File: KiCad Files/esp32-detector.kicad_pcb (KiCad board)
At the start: 4 copper layers, 89 parts, among them IC1 MC34119, J1 Coils Connector, J2 INTERFACE, U1 4066, U2 MCP602, U3 MCP602, U4 MCP602, U5 ESP32-WROOM-32, U6 LD1117S50TR, U7 LD1117S33TR

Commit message: Upload Schematic and PCB files
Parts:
- moved U6 45.5 mm to (74.2, 61.3)
- moved R30 36.7 mm to (107.1, 48.5), turned to 0 degrees
- moved H3 35.4 mm to (124.0, 70.0)
- moved R6 35.0 mm to (110.0, 28.6), turned to 180 degrees
- moved C2 34.2 mm to (115.0, 30.0)
- moved H2 34.1 mm to (124.0, 27.0)
- moved R29 32.5 mm to (107.1, 51.6)
- moved R7 32.4 mm to (115.0, 36.0), turned to 90 degrees
- moved C13 25.2 mm to (116.3, 40.6)
- moved C40 24.0 mm to (103.8, 41.0), turned to 0 degrees
- moved C39 23.9 mm to (103.8, 44.7), turned to 180 degrees
- moved C28 23.9 mm to (112.4, 45.2), turned to -90 degrees
- moved J2 23.4 mm to (103.9, 63.8)
- moved U7 22.7 mm to (114.0, 58.7)
- moved C38 21.9 mm to (119.6, 54.9)
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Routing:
- net /IO27: track 4.15 -> 60.6 mm, vias 0 -> 2
- net /EN: track 0.00 -> 51.9 mm, vias 0 -> 1
- net /TX_PIN: track 0.00 -> 49.8 mm, vias 0 -> 2
- net GND: track 65.4 -> 89.9 mm, vias 32 -> 39
- net /SENSOR_VN: track 0.00 -> 24.2 mm, vias 0 -> 1
- net Net-(C8-Pad1): track 0.00 -> 21.5 mm, vias 0 -> 1
- net Net-(C39-Pad1): track 0.00 -> 19.8 mm
- net RX_R: track 12.2 -> 28.6 mm, vias 0 -> 1
- net Net-(C2-Pad1): track 0.00 -> 16.2 mm, vias 0 -> 1
- net Vref: track 0.00 -> 15.3 mm, vias 0 -> 1
- net /IO0: track 4.96 -> 19.2 mm
- net /+3V3: track 18.4 -> 4.24 mm, vias 0 -> 1
- net Net-(C2-Pad2): track 0.00 -> 13.7 mm
- net /TXD: track 0.00 -> 11.6 mm
- net +5V: track 19.0 -> 8.47 mm, vias 4 -> 2
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- added copper zone on B.Cu, net +12V
- added copper zone on B.Cu, net +5V
- added copper zone on B.Cu, net /+3V3
- added copper zone on In1.Cu, net GND
- removed copper zone on In1.Cu, net +5V

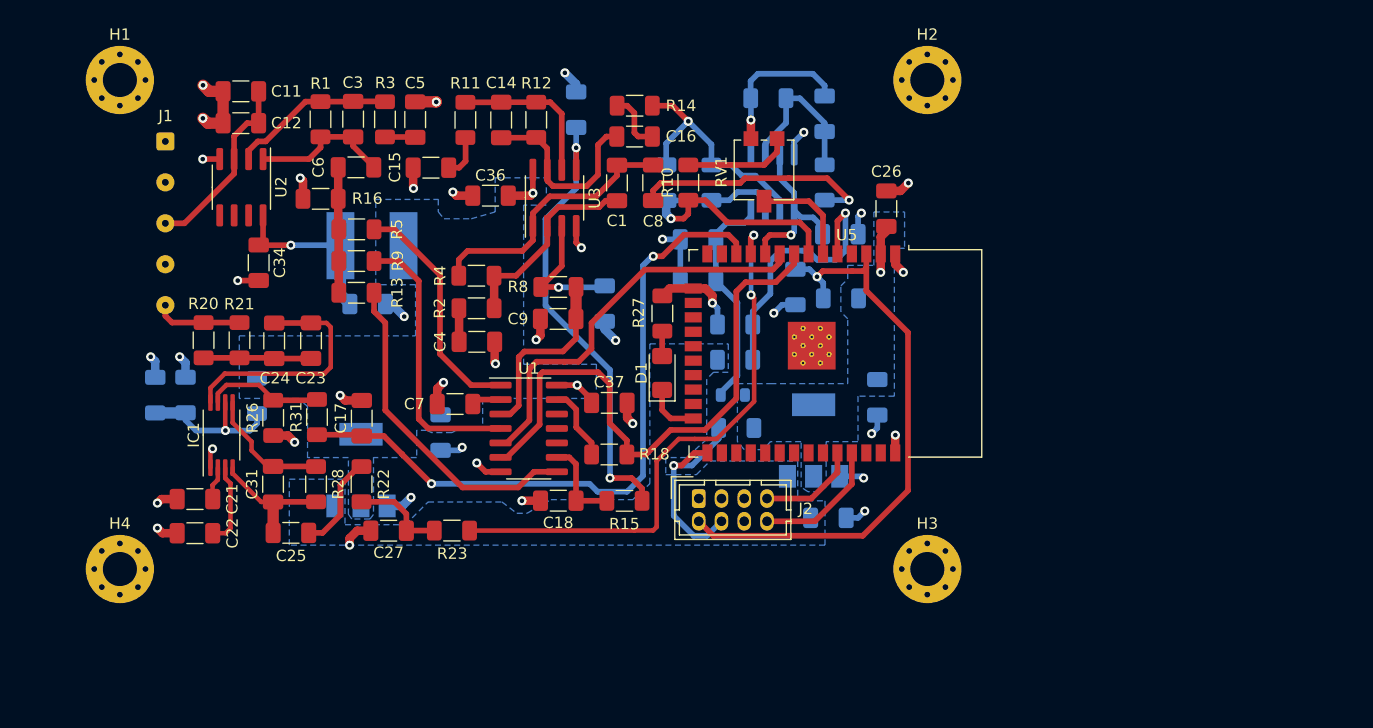
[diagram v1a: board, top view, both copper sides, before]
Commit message: Update sch and pcb files, Create .gitignore
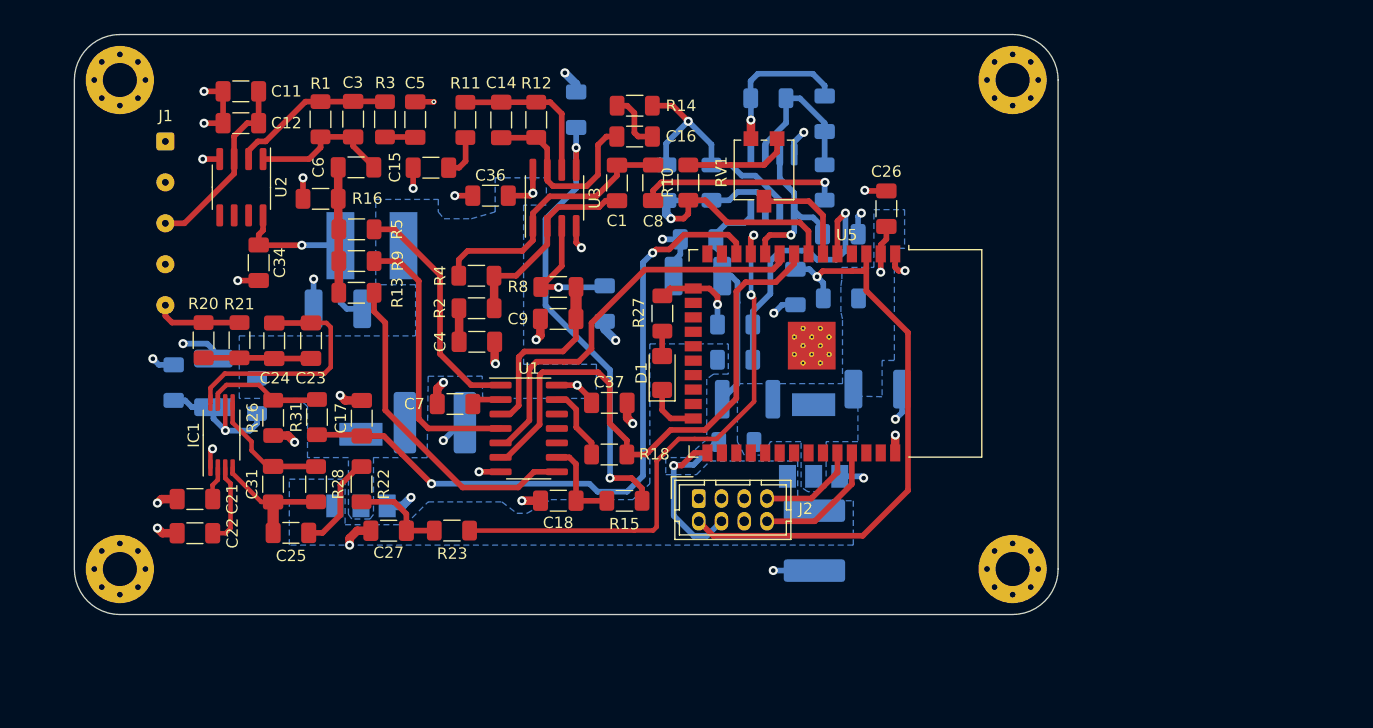
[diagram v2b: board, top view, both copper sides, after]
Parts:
- C29, C33, C38, C39: footprint Capacitor_SMD:C_1206_3216Metric_Pad1.33x1.80mm_HandSolder -> Capacitor_SMD:C_1812_4532Metric_Pad1.57x3.40mm_HandSolder
- C32, C35: footprint Capacitor_SMD:C_1206_3216Metric_Pad1.33x1.80mm_HandSolder -> Capacitor_SMD:C_2220_5650Metric_Pad1.97x5.40mm_HandSolder
- L1: footprint Inductor_SMD:L_0805_2012Metric -> Inductor_SMD:L_1812_4532Metric_Pad1.30x3.40mm_HandSolder
- moved H2 7.50 mm to (131.5, 27.0)
- moved H3 7.50 mm to (131.5, 70.0)
- moved C29 2.68 mm to (61.2, 53.6)
- moved C33 2.65 mm to (72.2, 47.1), turned to 180 degrees
- moved C32 2.35 mm to (114.1, 67.5), turned to -90 degrees
- moved C30 1.96 mm to (57.7, 53.6)
- moved L1 1.34 mm to (108.2, 55.1)
- moved R25 1.23 mm to (107.2, 58.8)
- moved C35 1.00 mm to (80.7, 57.1), turned to 0 degrees
- moved C38 0.72 mm to (119.6, 54.2), turned to 0 degrees
- moved C39 0.44 mm to (103.8, 44.2)
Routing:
- net GND: track 89.9 -> 93.7 mm
- net Net-(C8-Pad1): track 21.5 -> 17.9 mm
- net Net-(C33-Pad1): track 15.4 -> 17.1 mm
- net /IO0: track 19.2 -> 18.1 mm
- net Net-(C39-Pad1): track 19.8 -> 20.8 mm
- net Net-(C29-Pad1): track 13.6 -> 12.6 mm
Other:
- board outline added: 86.5 x 51 mm

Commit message: Via improvement
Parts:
- moved H2 5.00 mm to (126.5, 27.0)
- moved H3 5.00 mm to (126.5, 70.0)
- moved C21 4.49 mm to (58.5, 59.5), turned to 90 degrees
- moved H1 3.00 mm to (56.0, 27.0)
- moved H4 3.00 mm to (56.0, 70.0)
- moved C38 2.48 mm to (119.5, 51.7)
- moved C22 1.85 mm to (59.6, 65.0)
- moved L1 1.69 mm to (106.5, 55.1)
- moved C35 1.18 mm to (81.5, 58.0), turned to -90 degrees
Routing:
- net GND: track 93.7 -> 68.1 mm, vias 39 -> 41
- net Net-(C22-Pad2): track 7.27 -> 4.37 mm
- net Net-(C21-Pad1): track 2.97 -> 5.57 mm
- net Net-(C39-Pad1): track 20.8 -> 21.7 mm
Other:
- board size 86.5 x 51 mm -> 79 x 52 mm
